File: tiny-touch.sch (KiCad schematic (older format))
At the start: 28 parts, among them IC1 STM32F072VBT6, P1 Tiny-Touch-Pad, U1 MCP1700-3002E_SOT23, U2 SRV05-4

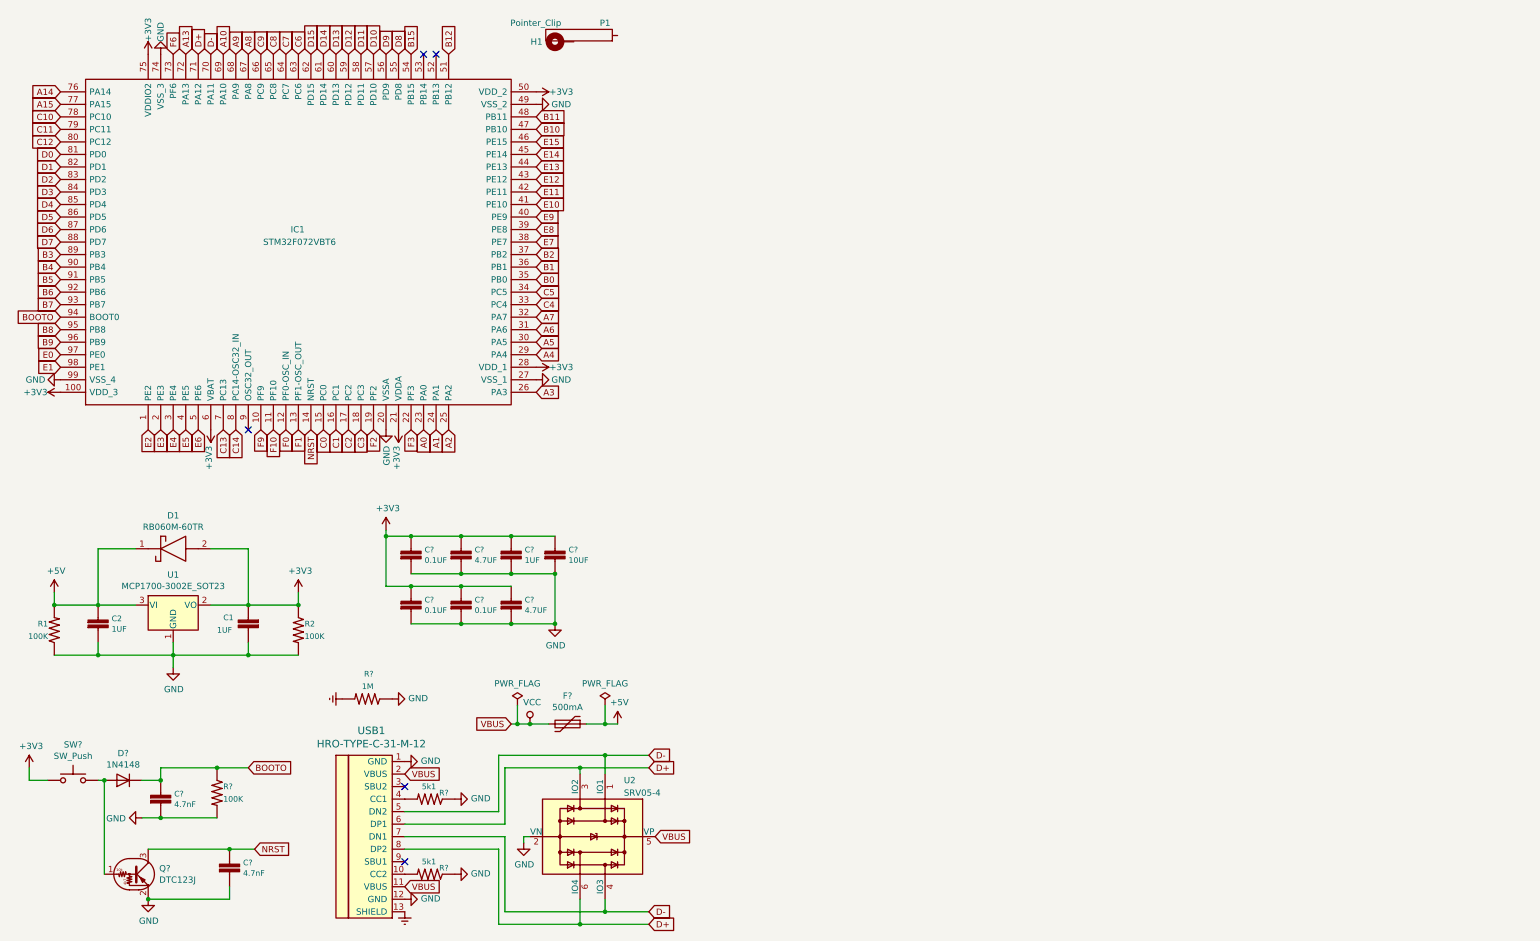
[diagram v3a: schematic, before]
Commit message: Add and label key pads
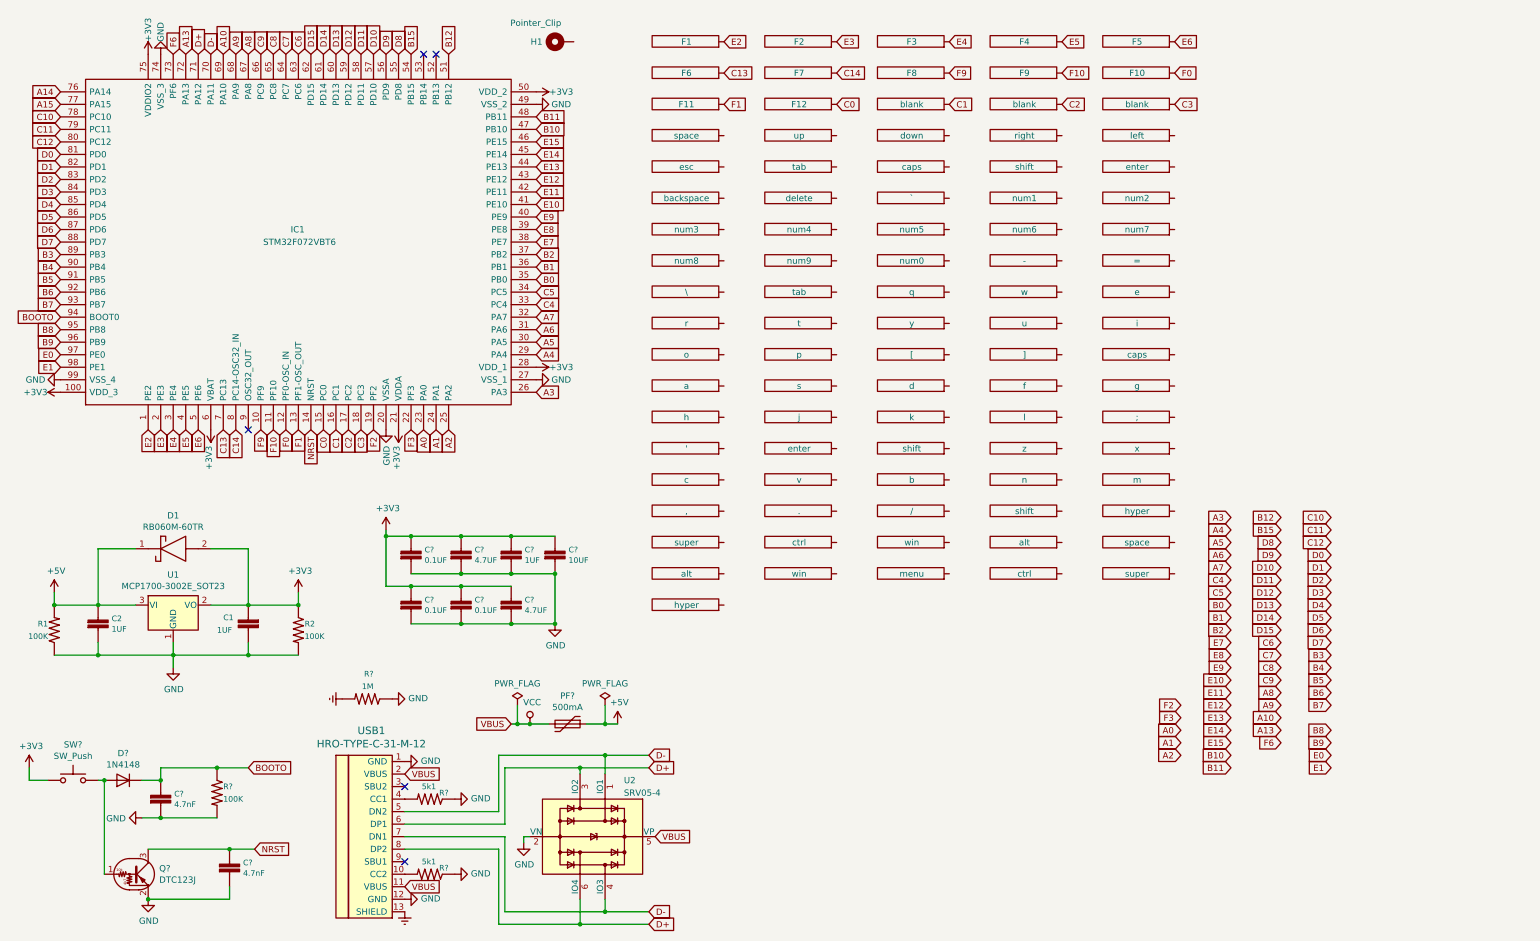
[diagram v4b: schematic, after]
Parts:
- removed P1: Tiny-Touch-Pad, symbol cKeys-symbols:Tiny-Touch-Pad
- added ', ,, -, ., /, ;, =, F1, F10, F11, F12, F2, F3, F4, F5, F6, F7, F8, F9, [, \, ], `, a, alt (x2), b, backspace, blank (x3), c, caps (x2), ctrl (x2), d, delete, down, e, enter (x2), esc, f, g, h, hyper (x2), i, j, k, l, left, m, menu, n, num0, num1, num2, num3, num4, num5, num6, num7, num8, num9, o, p, q, r, right, s, shift (x3), space (x2), super (x2), t, tab (x2), u, up, v, w, win (x2), x, y, z: Tiny-Touch-Pad, ckeys:Tiny-Touch-Pad, symbol cKeys-symbols:Tiny-Touch-Pad
- gave numbers to parts that had none: 1
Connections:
- net C0: now also F12.1
- net C1: now also blank.1
- net C13: now also F6.1
- net C14: now also F7.1
- net C2: now also blank.1
- net C3: now also blank.1
- net E2: now also F1.1
- net E3: now also F2.1
- net E4: now also F3.1
- net E5: now also F4.1
- net E6: now also F5.1
- net F0: now also F10.1
- net F1: now also F11.1
- net F10: now also F9.1
- net F9: now also F8.1
